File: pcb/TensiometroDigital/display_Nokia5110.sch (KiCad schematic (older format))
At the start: 2 parts

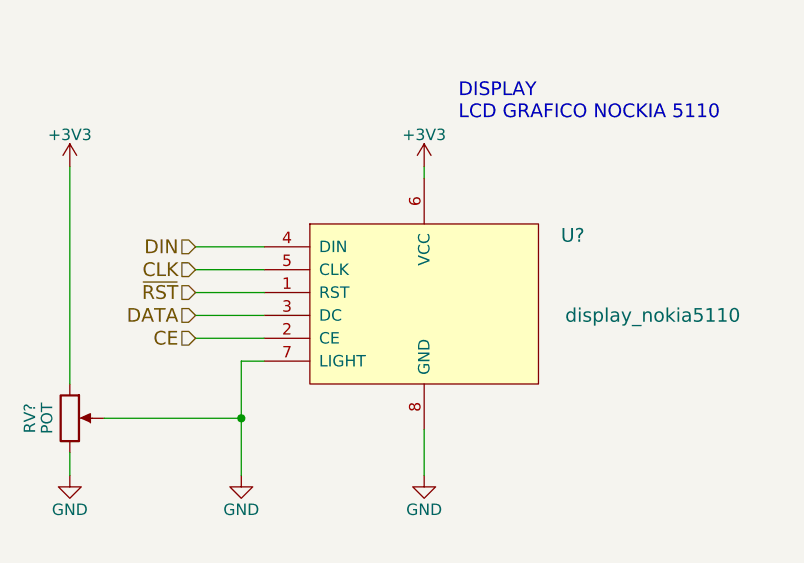
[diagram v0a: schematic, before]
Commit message: Finalizado: SCH, PCB, GABINETE, DRAWINGS. FALTA: GERBERS, BOM e Informe
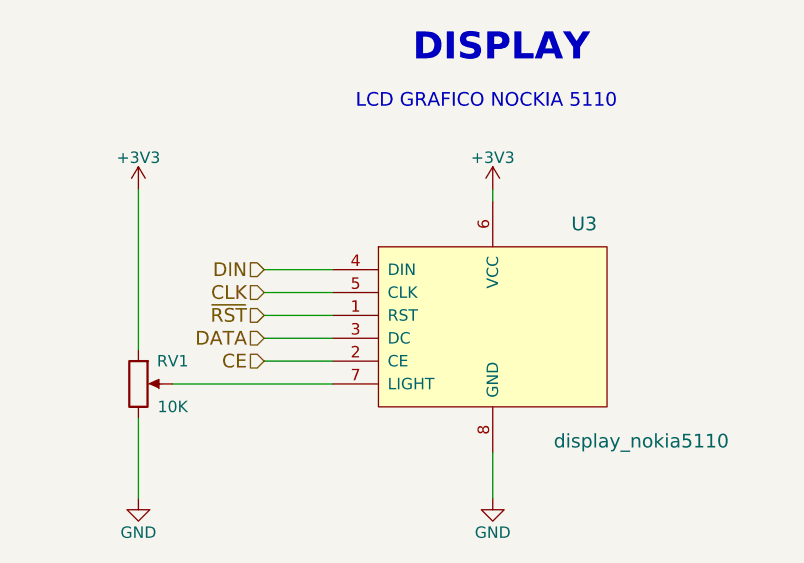
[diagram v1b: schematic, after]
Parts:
- RV1: renamed from RV?; value POT -> 10K; footprint (none) -> Potentiometers:Potentiometer_Trimmer_Bourns_3296W
- U3: renamed from U?; footprint (none) -> Socket_Strips:Socket_Strip_Straight_1x08_Pitch2.54mm; manf# (none) -> LCD-10168
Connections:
- net GND: no longer RV1.2, U3.7 (LIGHT)
- new net: RV1.2, U3.7 (LIGHT)
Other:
- note added: "DISPLAY"
- note added: "LCD GRAFICO NOCKIA 5110"
- note removed: "DISPLAY\nLCD GRAFICO NOCKIA 5110"
- moved on the sheet: RV1, U3
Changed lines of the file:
@@
 LIBS:lm2940
 LIBS:lm2575
+LIBS:bav199
+LIBS:mpxv5050gp
+LIBS:lm8364
 LIBS:TensiometroDigital-cache
 EELAYER 25 0
@@
 $Descr A4 11693 8268
 encoding utf-8
-Sheet 3 8
-Title ""
-Date ""
-Rev ""
-Comp ""
-Comment1 ""
-Comment2 ""
-Comment3 ""
-Comment4 ""
+Sheet 2 11
+Title "TENSIÓMETRO DIGITAL"
+Date "2018-11-20"
+Rev "A"
+Comp "UTN - FRBA"
+Comment1 "Curso: R1032"
+Comment2 "Leg.: 153204-2"
+Comment3 "Autor: Alegre Mendoza Ezequiel"
+Comment4 "SDR Proyecto Final"
 $EndDescr
-Text Notes 5750 3050 0    60   ~ 0
-DISPLAY\nLCD GRAFICO NOCKIA 5110
+Text Notes 5300 3000 0    60   ~ 0
+LCD GRAFICO NOCKIA 5110
 $Comp
-L display_nokia5110 U?
+L display_nokia5110 U3
 U 1 1 5BBE51BA
-P 5100 3500
-F 0 "U?" H 6250 3450 60  0000 C CNN
-F 1 "display_nokia5110" H 6600 3100 60  0000 C CNN
-F 2 "" H 5100 3500 60  0001 C CNN
-F 3 "" H 5100 3500 60  0001 C CNN
-	1    5100 3500
+P 5400 3600
+F 0 "U3" H 6300 3700 60  0000 C CNN
+F 1 "display_nokia5110" H 6550 2750 60  0000 C CNN
+F 2 "Socket_Strips:Socket_Strip_Straight_1x08_Pitch2.54mm" H 5400 3600 60  0001 C CNN
+F 3 "" H 5400 3600 60  0001 C CNN
+F 4 "LCD-10168" H 5400 3600 60  0001 C CNN "manf#"
+	1    5400 3600
 	1    0    0    -1
 $EndComp
 $Comp
-L GND #PWR?
+L GND #PWR01
 U 1 1 5BBE51D6
-P 5600 4600
-F 0 "#PWR?" H 5600 4350 50  0001 C CNN
-F 1 "GND" H 5600 4450 50  0000 C CNN
-F 2 "" H 5600 4600 50  0001 C CNN
-F 3 "" H 5600 4600 50  0001 C CNN
-	1    5600 4600
+P 5900 4700
+F 0 "#PWR01" H 5900 4450 50  0001 C CNN
+F 1 "GND" H 5900 4550 50  0000 C CNN
+F 2 "" H 5900 4700 50  0001 C CNN
+F 3 "" H 5900 4700 50  0001 C CNN
+	1    5900 4700
 	1    0    0    -1
 $EndComp
-Text HLabel 4600 3600 0    60   Input ~ 0
+Text HLabel 4900 3700 0    60   Input ~ 0
 DIN
-Text HLabel 4600 3700 0    60   Input ~ 0
+Text HLabel 4900 3800 0    60   Input ~ 0
 CLK
-Text HLabel 4600 3800 0    60   Input ~ 0
+Text HLabel 4900 3900 0    60   Input ~ 0
 ~RST
-Text HLabel 4600 3900 0    60   Input ~ 0
+Text HLabel 4900 4000 0    60   Input ~ 0
 DATA
-Text HLabel 4600 4000 0    60   Input ~ 0
+Text HLabel 4900 4100 0    60   Input ~ 0
 CE
 $Comp
-L GND #PWR?
-U 1 1 5BBE5579
-P 4800 4600
-F 0 "#PWR?" H 4800 4350 50  0001 C CNN
-F 1 "GND" H 4800 4450 50  0000 C CNN
-F 2 "" H 4800 4600 50  0001 C CNN
-F 3 "" H 4800 4600 50  0001 C CNN
-	1    4800 4600
+L POT RV1
+U 1 1 5BBE569A
+P 4350 4200
+F 0 "RV1" H 4500 4300 50  0000 C CNN
+F 1 "10K" H 4500 4100 50  0000 C CNN
+F 2 "Potentiometers:Potentiometer_Trimmer_Bourns_3296W" H 4350 4200 50  0001 C CNN
+F 3 "3296W-1-103LF" H 4350 4200 50  0001 C CNN
+	1    4350 4200
 	1    0    0    -1
 $EndComp
 $Comp
-L POT RV?
-U 1 1 5BBE569A
-P 4050 4350
-F 0 "RV?" V 3875 4350 50  0000 C CNN
-F 1 "POT" V 3950 4350 50  0000 C CNN
-F 2 "" H 4050 4350 50  0001 C CNN
-F 3 "" H 4050 4350 50  0001 C CNN
-	1    4050 4350
+L GND #PWR02
+U 1 1 5BBE56DD
+P 4350 4700
+F 0 "#PWR02" H 4350 4450 50  0001 C CNN
+F 1 "GND" H 4350 4550 50  0000 C CNN
+F 2 "" H 4350 4700 50  0001 C CNN
+F 3 "" H 4350 4700 50  0001 C CNN
+	1    4350 4700
 	1    0    0    -1
 $EndComp
 $Comp
-L GND #PWR?
-U 1 1 5BBE56DD
-P 4050 4600
-F 0 "#PWR?" H 4050 4350 50  0001 C CNN
-F 1 "GND" H 4050 4450 50  0000 C CNN
-F 2 "" H 4050 4600 50  0001 C CNN
-F 3 "" H 4050 4600 50  0001 C CNN
-	1    4050 4600
+L +3V3 #PWR03
+U 1 1 5BC1199C
+P 4350 3350
+F 0 "#PWR03" H 4350 3200 50  0001 C CNN
+F 1 "+3V3" H 4350 3490 50  0000 C CNN
+F 2 "" H 4350 3350 50  0001 C CNN
+F 3 "" H 4350 3350 50  0001 C CNN
+	1    4350 3350
 	1    0    0    -1
 $EndComp
 $Comp
-L +3V3 #PWR?
-U 1 1 5BC1199C
-P 4050 3250
-F 0 "#PWR?" H 4050 3100 50  0001 C CNN
-F 1 "+3V3" H 4050 3390 50  0000 C CNN
-F 2 "" H 4050 3250 50  0001 C CNN
-F 3 "" H 4050 3250 50  0001 C CNN
-	1    4050 3250
-	1    0    0    -1
-$EndComp
-$Comp
-L +3V3 #PWR?
+L +3V3 #PWR04
 U 1 1 5BC119B4
-P 5600 3250
-F 0 "#PWR?" H 5600 3100 50  0001 C CNN
-F 1 "+3V3" H 5600 3390 50  0000 C CNN
-F 2 "" H 5600 3250 50  0001 C CNN
-F 3 "" H 5600 3250 50  0001 C CNN
-	1    5600 3250
+P 5900 3350
+F 0 "#PWR04" H 5900 3200 50  0001 C CNN
+F 1 "+3V3" H 5900 3490 50  0000 C CNN
+F 2 "" H 5900 3350 50  0001 C CNN
+F 3 "" H 5900 3350 50  0001 C CNN
+	1    5900 3350
 	1    0    0    -1
 $EndComp
 Wire Wire Line
-	5600 4600 5600 4400
+	5900 4700 5900 4500
 Wire Wire Line
-	5600 3250 5600 3300
+	5900 3350 5900 3400
 Wire Wire Line
-	4900 3600 4600 3600
+	5200 3700 4900 3700
 Wire Wire Line
-	4900 3700 4600 3700
+	5200 3800 4900 3800
 Wire Wire Line
-	4900 3800 4600 3800
+	5200 3900 4900 3900
 Wire Wire Line
-	4900 3900 4600 3900
+	5200 4000 4900 4000
 Wire Wire Line
-	4900 4000 4600 4000
+	5200 4100 4900 4100
 Wire Wire Line
-	4900 4100 4800 4100
+	4500 4200 5200 4200
 Wire Wire Line
-	4800 4100 4800 4350
+	4350 4700 4350 4350
 Wire Wire Line
-	4800 4350 4800 4600
+	4350 4050 4350 3350
+Text Notes 5550 2800 0    118  ~ 24
+DISPLAY
 Wire Wire Line
-	4050 4600 4050 4500
-Wire Wire Line
-	4050 4200 4050 3250
-Wire Wire Line
-	4800 4350 4200 4350
-Connection ~ 4800 4350
+	5100 4200 5100 4200
 $EndSCHEMATC
